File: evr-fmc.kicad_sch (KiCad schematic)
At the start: 0 parts

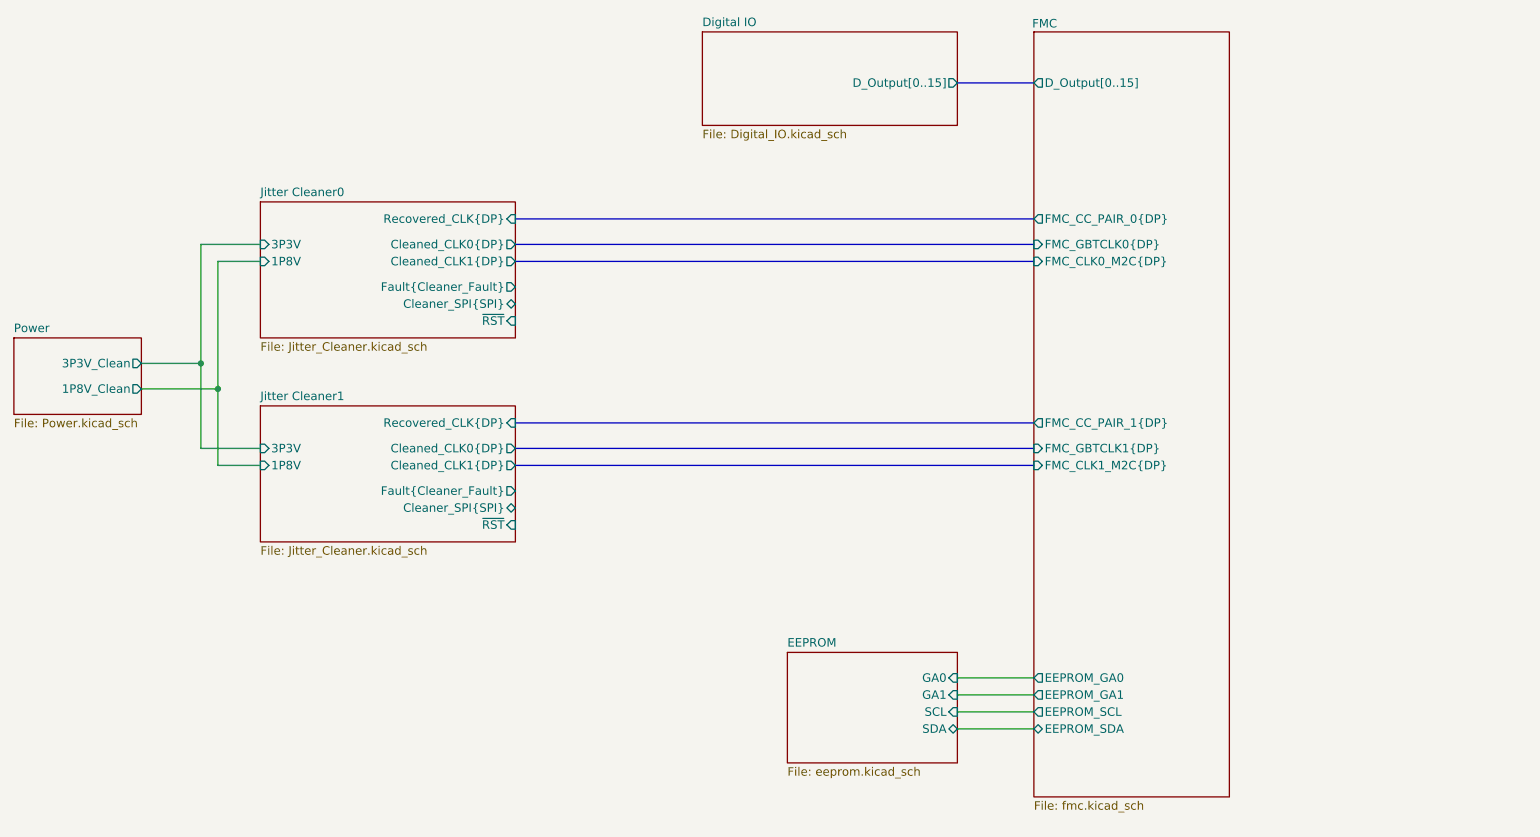
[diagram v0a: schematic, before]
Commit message: Completed Schematic
Completed Schematic Draft
- Includes careful pin mapping to avoid conflicts with other firmwares
- Roughed out LCB layout high speed traces, and FMC breakouts.

Layout and BOM are still WIP
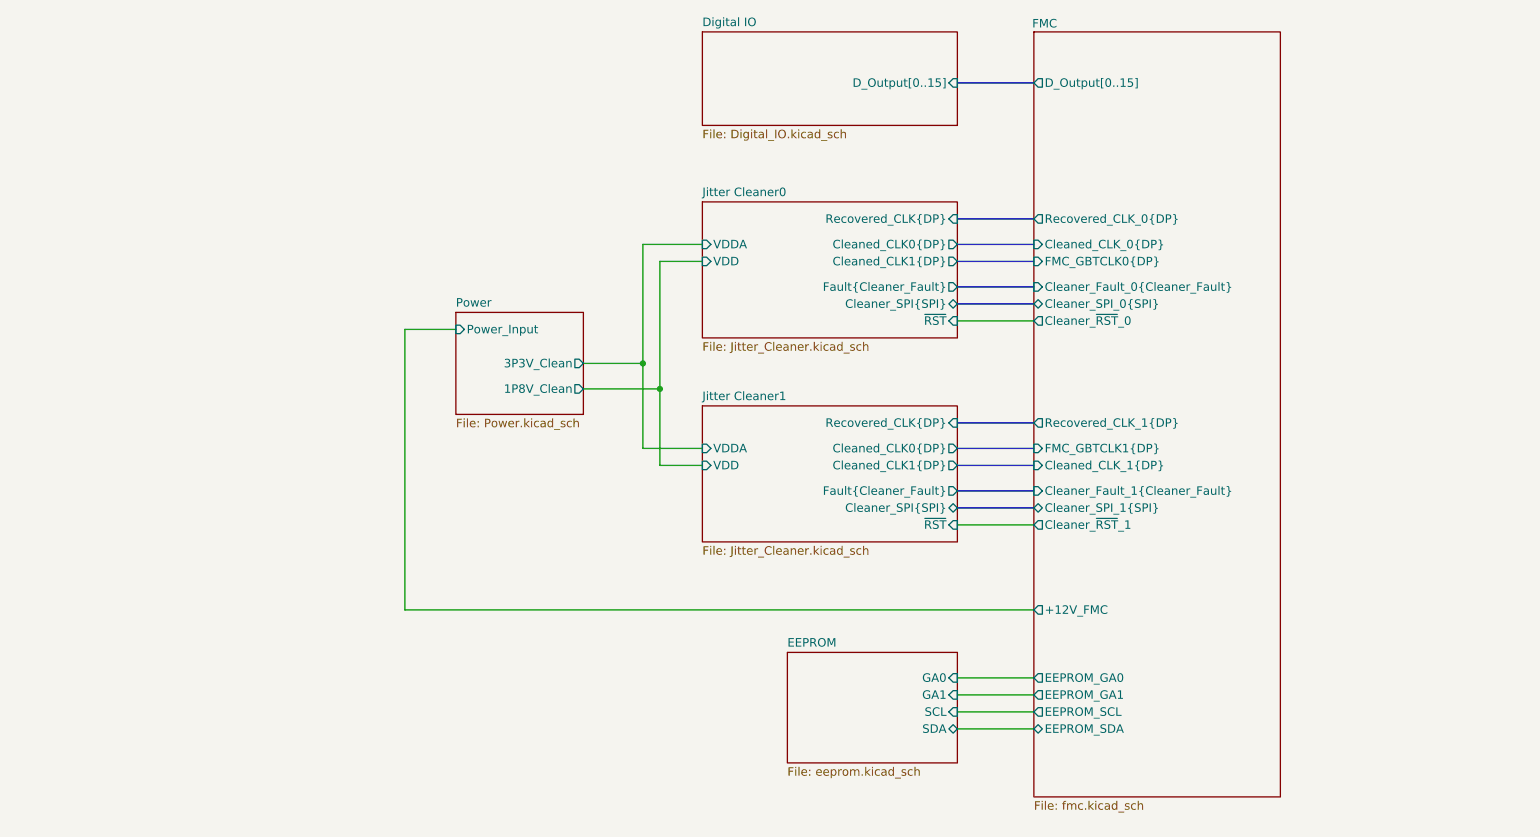
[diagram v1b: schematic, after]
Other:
- sheet FMC ports: added +12V_FMC, Cleaned_CLK_0{DP}, Cleaned_CLK_1{DP}, Cleaner_Fault_0{Cleaner_Fault}, Cleaner_Fault_1{Cleaner_Fault}, Cleaner_SPI_0{SPI}, Cleaner_SPI_1{SPI}, Cleaner_~{RST}_0, Cleaner_~{RST}_1, Recovered_CLK_0{DP}, Recovered_CLK_1{DP}; removed FMC_CC_PAIR_0{DP}, FMC_CC_PAIR_1{DP}, FMC_CLK0_M2C{DP}, FMC_CLK1_M2C{DP}
- sheet Jitter Cleaner0 ports: added VDD, VDDA; removed 1P8V, 3P3V
- sheet Jitter Cleaner1 ports: added VDD, VDDA; removed 1P8V, 3P3V
- sheet Power ports: added Power_Input; removed none

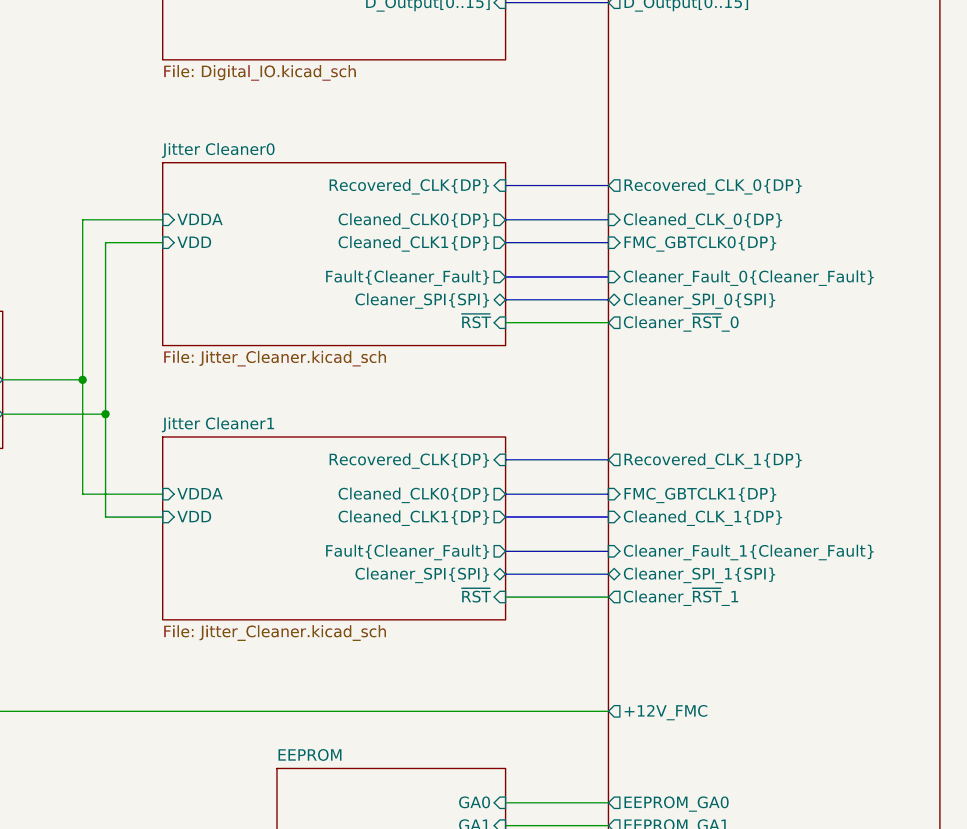
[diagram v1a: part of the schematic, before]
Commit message: Schematic Updates
-Added Heartbeat LED
-Assigned Jitter cleaner OE to FPGA pins
-Changed LDO parts
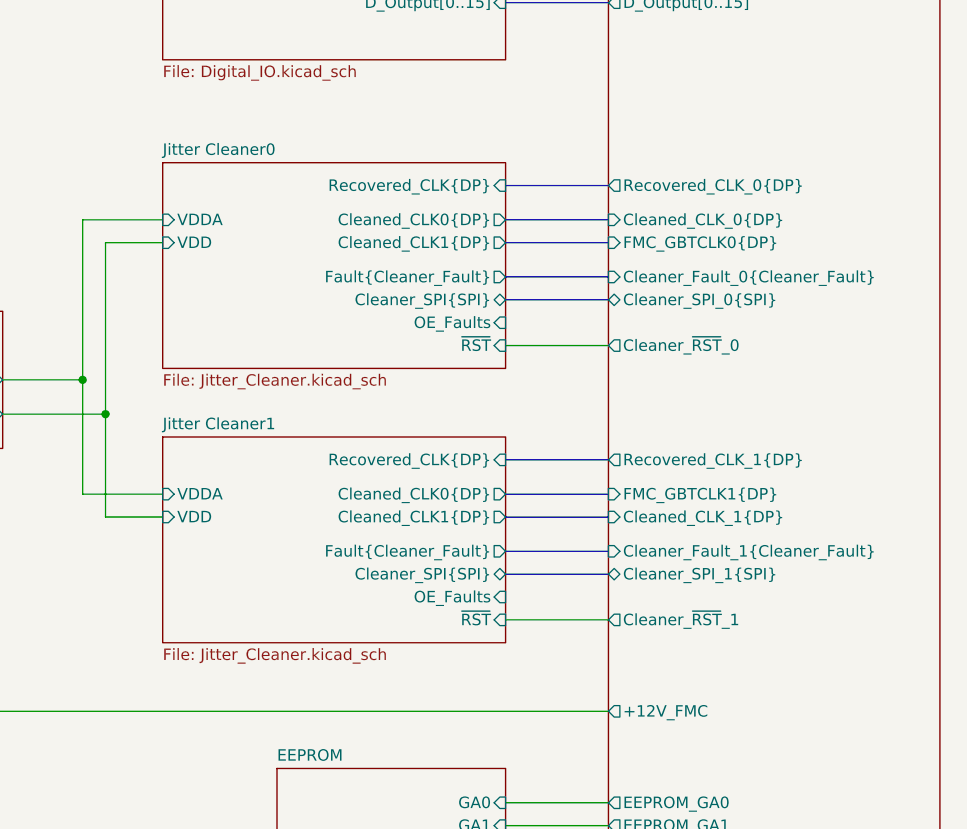
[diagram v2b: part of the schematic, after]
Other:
- sheet Jitter Cleaner0 ports: added OE_Faults; removed none
- sheet Jitter Cleaner1 ports: added OE_Faults; removed none
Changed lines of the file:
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@@
 	(wire
 		(pts
-			(xy 161.29 113.03) (xy 172.72 113.03)
+			(xy 161.29 115.57) (xy 172.72 115.57)
 		)
 		(stroke
@@
 	(wire
 		(pts
-			(xy 161.29 82.55) (xy 172.72 82.55)
+			(xy 161.29 85.09) (xy 172.72 85.09)
 		)
 		(stroke
@@
 	(sheet
 		(at 123.19 95.25)
-		(size 38.1 20.32)
+		(size 38.1 22.86)
 		(exclude_from_sim no)
 		(in_bom yes)
@@
 		)
 		(property "Sheetfile" "Jitter_Cleaner.kicad_sch"
-			(at 123.19 116.1546 0)
+			(at 123.19 118.6946 0)
 			(effects
 				(font
@@
 		)
 		(pin "~{RST}" input
-			(at 161.29 113.03 0)
+			(at 161.29 115.57 0)
 			(effects
 				(font
@@
 				)
 				(justify left)
+			)
+		)
+		(pin "OE_Faults" input
+			(at 161.29 113.03 0)
+			(effects
+				(font
+					(size 1.27 1.27)
+				)
+				(justify right)
 			)
 		)
@@
 	(sheet
 		(at 123.19 64.77)
-		(size 38.1 20.32)
+		(size 38.1 22.86)
 		(exclude_from_sim no)
 		(in_bom yes)
@@
 		)
 		(property "Sheetfile" "Jitter_Cleaner.kicad_sch"
-			(at 123.19 85.6746 0)
+			(at 123.19 88.2146 0)
 			(effects
 				(font
@@
 		)
 		(pin "~{RST}" input
-			(at 161.29 82.55 0)
+			(at 161.29 85.09 0)
 			(effects
 				(font
@@
 				)
 				(justify left)
+			)
+		)
+		(pin "OE_Faults" input
+			(at 161.29 82.55 0)
+			(effects
+				(font
+					(size 1.27 1.27)
+				)
+				(justify right)
 			)
 		)
@@
 		)
 		(pin "Cleaner_~{RST}_0" output
-			(at 172.72 82.55 180)
+			(at 172.72 85.09 180)
 			(effects
 				(font
@@
 		)
 		(pin "Cleaner_~{RST}_1" output
-			(at 172.72 113.03 180)
-			(effects
-				(font
+			(at 172.72 115.57 180)
+			(effects
+				(font

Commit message: Finalized Schematic and Updated Layout
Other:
- sheet Power ports: added 1P8V_Clean_0, 1P8V_Clean_1, 3P3V_Clean_0, 3P3V_Clean_1; removed 1P8V_Clean, 3P3V_Clean
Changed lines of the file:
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@@
 		(members "P" "N")
 	)
-	(junction
-		(at 116.84 92.71)
-		(diameter 0)
-		(color 0 0 0 0)
-	)
-	(junction
-		(at 114.3 88.9)
-		(diameter 0)
-		(color 0 0 0 0)
-	)
 	(wire
 		(pts
@@
 	(wire
 		(pts
-			(xy 123.19 101.6) (xy 114.3 101.6)
-		)
-		(stroke
-			(width 0)
-			(type default)
-		)
-	)
-	(wire
-		(pts
 			(xy 161.29 115.57) (xy 172.72 115.57)
 		)
@@
 	(wire
 		(pts
-			(xy 114.3 88.9) (xy 105.41 88.9)
-		)
-		(stroke
-			(width 0)
-			(type default)
-		)
-	)
-	(wire
-		(pts
-			(xy 114.3 71.12) (xy 114.3 88.9)
-		)
-		(stroke
-			(width 0)
-			(type default)
-		)
-	)
-	(wire
-		(pts
-			(xy 116.84 104.14) (xy 116.84 92.71)
-		)
-		(stroke
-			(width 0)
-			(type default)
-		)
-	)
-	(wire
-		(pts
-			(xy 123.19 104.14) (xy 116.84 104.14)
-		)
-		(stroke
-			(width 0)
-			(type default)
-		)
-	)
-	(wire
-		(pts
-			(xy 114.3 101.6) (xy 114.3 88.9)
+			(xy 114.3 83.82) (xy 105.41 83.82)
+		)
+		(stroke
+			(width 0)
+			(type default)
+		)
+	)
+	(wire
+		(pts
+			(xy 114.3 71.12) (xy 114.3 83.82)
+		)
+		(stroke
+			(width 0)
+			(type default)
+		)
+	)
+	(wire
+		(pts
+			(xy 114.3 95.25) (xy 114.3 104.14)
 		)
 		(stroke
@@
 	(wire
 		(pts
-			(xy 78.74 83.82) (xy 86.36 83.82)
-		)
-		(stroke
-			(width 0)
-			(type default)
-		)
-	)
-	(wire
-		(pts
-			(xy 116.84 73.66) (xy 116.84 92.71)
+			(xy 78.74 80.01) (xy 86.36 80.01)
+		)
+		(stroke
+			(width 0)
+			(type default)
+		)
+	)
+	(wire
+		(pts
+			(xy 116.84 73.66) (xy 116.84 86.36)
+		)
+		(stroke
+			(width 0)
+			(type default)
+		)
+	)
+	(wire
+		(pts
+			(xy 116.84 101.6) (xy 123.19 101.6)
 		)
 		(stroke
@@
 	(wire
 		(pts
+			(xy 114.3 104.14) (xy 123.19 104.14)
+		)
+		(stroke
+			(width 0)
+			(type default)
+		)
+	)
+	(wire
+		(pts
 			(xy 161.29 140.97) (xy 172.72 140.97)
 		)
@@
 	(wire
 		(pts
-			(xy 116.84 92.71) (xy 105.41 92.71)
+			(xy 116.84 86.36) (xy 105.41 86.36)
 		)
 		(stroke
@@
 	(wire
 		(pts
-			(xy 78.74 125.73) (xy 78.74 83.82)
+			(xy 78.74 125.73) (xy 78.74 80.01)
+		)
+		(stroke
+			(width 0)
+			(type default)
+		)
+	)
+	(wire
+		(pts
+			(xy 105.41 92.71) (xy 116.84 92.71)
 		)
 		(stroke
@@
 		)
 	)
+	(wire
+		(pts
+			(xy 116.84 92.71) (xy 116.84 101.6)
+		)
+		(stroke
+			(width 0)
+			(type default)
+		)
+	)
 	(bus
 		(pts
@@
 		(pts
 			(xy 161.29 71.12) (xy 172.72 71.12)
+		)
+		(stroke
+			(width 0)
+			(type default)
+		)
+	)
+	(wire
+		(pts
+			(xy 105.41 95.25) (xy 114.3 95.25)
 		)
 		(stroke
@@
 	)
 	(sheet
-		(at 86.36 81.28)
-		(size 19.05 15.24)
+		(at 86.36 77.47)
+		(size 19.05 21.59)
 		(exclude_from_sim no)
 		(in_bom yes)
@@
 		)
 		(property "Sheetname" "Power"
-			(at 86.36 80.5684 0)
+			(at 86.36 76.7584 0)
 			(effects
 				(font
@@
 		)
 		(property "Sheetfile" "Power.kicad_sch"
-			(at 86.36 97.1046 0)
+			(at 86.36 99.6446 0)
 			(effects
 				(font
@@
 			)
 		)
-		(pin "1P8V_Clean" output
+		(pin "Power_Input" input
+			(at 86.36 80.01 180)
+			(effects
+				(font
+					(size 1.27 1.27)
+				)
+				(justify left)
+			)
+		)
+		(pin "1P8V_Clean_0" output
+			(at 105.41 86.36 0)
+			(effects
+				(font
+					(size 1.27 1.27)
+				)
+				(justify right)
+			)
+		)
+		(pin "1P8V_Clean_1" output
+			(at 105.41 95.25 0)
+			(effects
+				(font
+					(size 1.27 1.27)
+				)
+				(justify right)
+			)
+		)
+		(pin "3P3V_Clean_0" output
+			(at 105.41 83.82 0)
+			(effects
+				(font
+					(size 1.27 1.27)
+				)
+				(justify right)
+			)
+		)
+		(pin "3P3V_Clean_1" output
 			(at 105.41 92.71 0)
 			(effects
@@
 			)
 		)
-		(pin "3P3V_Clean" output
-			(at 105.41 88.9 0)
-			(effects
-				(font
-					(size 1.27 1.27)
-				)
-				(justify right)
-			)
-		)
-		(pin "Power_Input" input
-			(at 86.36 83.82 180)
-			(effects
-				(font
-					(size 1.27 1.27)
-				)
-				(justify left)
-			)
-		)

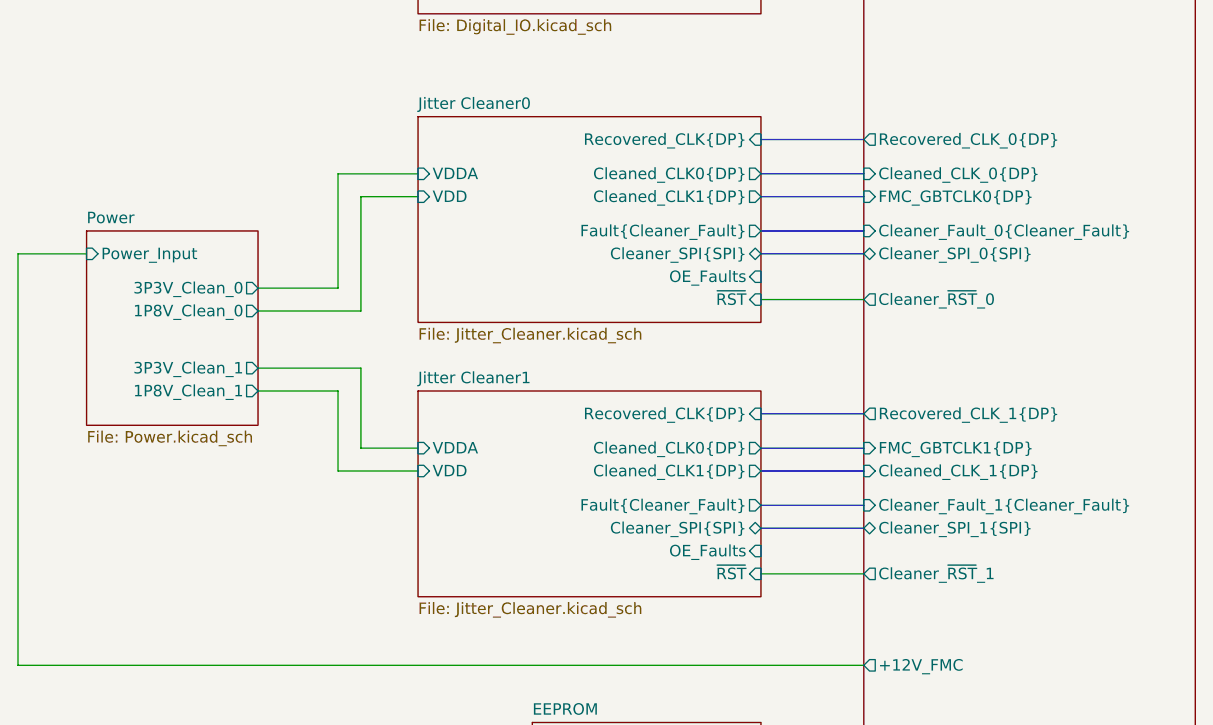
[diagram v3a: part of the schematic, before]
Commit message: Draft Layout Complete
-Draft Layout Complete
- Silkscreen need to be complete
- some Digital IO swapped FMC pins
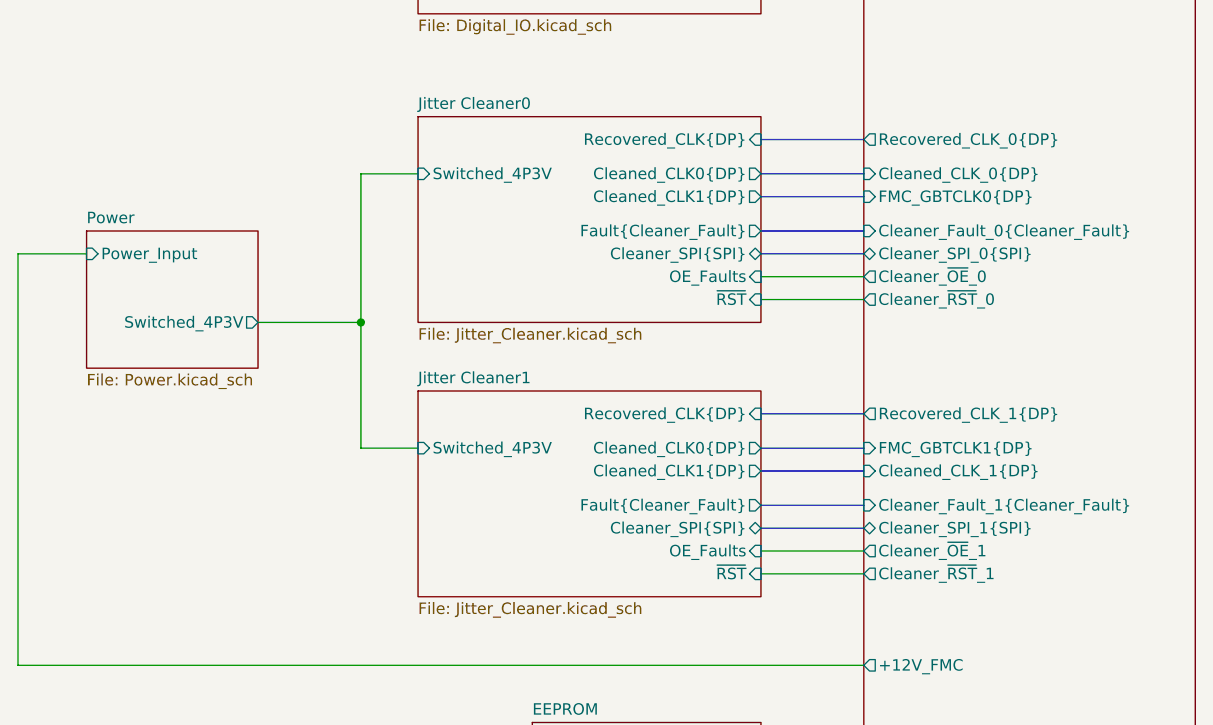
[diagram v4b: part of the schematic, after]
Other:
- sheet FMC ports: added Cleaner_~{OE}_0, Cleaner_~{OE}_1; removed none
- sheet Jitter Cleaner0 ports: added Switched_4P3V; removed VDD, VDDA
- sheet Jitter Cleaner1 ports: added Switched_4P3V; removed VDD, VDDA
- sheet Power ports: added Switched_4P3V; removed 1P8V_Clean_0, 1P8V_Clean_1, 3P3V_Clean_0, 3P3V_Clean_1
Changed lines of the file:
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@@
 		(members "P" "N")
 	)
+	(junction
+		(at 116.84 87.63)
+		(diameter 0)
+		(color 0 0 0 0)
+	)
 	(wire
 		(pts
@@
 	(wire
 		(pts
-			(xy 114.3 83.82) (xy 105.41 83.82)
-		)
-		(stroke
-			(width 0)
-			(type default)
-		)
-	)
-	(wire
-		(pts
-			(xy 114.3 71.12) (xy 114.3 83.82)
-		)
-		(stroke
-			(width 0)
-			(type default)
-		)
-	)
-	(wire
-		(pts
-			(xy 114.3 95.25) (xy 114.3 104.14)
+			(xy 116.84 71.12) (xy 116.84 87.63)
 		)
 		(stroke
@@
 	(wire
 		(pts
-			(xy 123.19 71.12) (xy 114.3 71.12)
+			(xy 123.19 71.12) (xy 116.84 71.12)
 		)
 		(stroke
@@
 	(wire
 		(pts
-			(xy 116.84 73.66) (xy 116.84 86.36)
+			(xy 161.29 82.55) (xy 172.72 82.55)
 		)
 		(stroke
@@
 		)
 	)
-	(wire
-		(pts
-			(xy 123.19 73.66) (xy 116.84 73.66)
-		)
-		(stroke
-			(width 0)
-			(type default)
-		)
-	)
 	(bus
 		(pts
@@
 	(wire
 		(pts
-			(xy 114.3 104.14) (xy 123.19 104.14)
-		)
-		(stroke
-			(width 0)
-			(type default)
-		)
-	)
-	(wire
-		(pts
 			(xy 161.29 140.97) (xy 172.72 140.97)
 		)
@@
 	(wire
 		(pts
-			(xy 116.84 86.36) (xy 105.41 86.36)
-		)
-		(stroke
-			(width 0)
-			(type default)
-		)
-	)
-	(wire
-		(pts
 			(xy 172.72 125.73) (xy 78.74 125.73)
 		)
@@
 	(wire
 		(pts
-			(xy 105.41 92.71) (xy 116.84 92.71)
+			(xy 105.41 87.63) (xy 116.84 87.63)
 		)
 		(stroke
@@
 	(wire
 		(pts
-			(xy 116.84 92.71) (xy 116.84 101.6)
+			(xy 116.84 87.63) (xy 116.84 101.6)
+		)
+		(stroke
+			(width 0)
+			(type default)
+		)
+	)
+	(wire
+		(pts
+			(xy 161.29 113.03) (xy 172.72 113.03)
 		)
 		(stroke
@@
 		(pts
 			(xy 161.29 71.12) (xy 172.72 71.12)
-		)
-		(stroke
-			(width 0)
-			(type default)
-		)
-	)
-	(wire
-		(pts
-			(xy 105.41 95.25) (xy 114.3 95.25)
 		)
 		(stroke
@@
 			)
 		)
-		(pin "VDD" input
-			(at 123.19 104.14 180)
-			(effects
-				(font
-					(size 1.27 1.27)
-				)
-				(justify left)
-			)
-		)
-		(pin "VDDA" input
-			(at 123.19 101.6 180)
-			(effects
-				(font
-					(size 1.27 1.27)
-				)
-				(justify left)
-			)
-		)
 		(pin "OE_Faults" input
 			(at 161.29 113.03 0)
@@
 				)
 				(justify right)
+			)
+		)
+		(pin "Switched_4P3V" input
+			(at 123.19 101.6 180)
+			(effects
+				(font
+					(size 1.27 1.27)
+				)
+				(justify left)
 			)
 		)
@@
 			)
 		)
-		(pin "VDD" input
-			(at 123.19 73.66 180)
-			(effects
-				(font
-					(size 1.27 1.27)
-				)
-				(justify left)
-			)
-		)
-		(pin "VDDA" input
-			(at 123.19 71.12 180)
-			(effects
-				(font
-					(size 1.27 1.27)
-				)
-				(justify left)
-			)
-		)
 		(pin "OE_Faults" input
 			(at 161.29 82.55 0)
@@
 				)
 				(justify right)
+			)
+		)
+		(pin "Switched_4P3V" input
+			(at 123.19 71.12 180)
+			(effects
+				(font
+					(size 1.27 1.27)
+				)
+				(justify left)
 			)
 		)
@@
 			)
 		)
+		(pin "Cleaner_~{OE}_0" output
+			(at 172.72 82.55 180)
+			(effects
+				(font
+					(size 1.27 1.27)
+				)
+				(justify left)
+			)
+		)
+		(pin "Cleaner_~{OE}_1" output
+			(at 172.72 113.03 180)
+			(effects
+				(font
+					(size 1.27 1.27)
+				)
+				(justify left)
+			)
+		)
 		(instances
 			(project "evr-fmc"
@@
 	(sheet
 		(at 86.36 77.47)
-		(size 19.05 21.59)
+		(size 19.05 15.24)
 		(exclude_from_sim no)
 		(in_bom yes)
@@
 		)
 		(property "Sheetfile" "Power.kicad_sch"
-			(at 86.36 99.6446 0)
+			(at 86.36 93.2946 0)
 			(effects
 				(font
@@
 			)
 		)
-		(pin "1P8V_Clean_0" output
-			(at 105.41 86.36 0)
-			(effects
-				(font
-					(size 1.27 1.27)
-				)
-				(justify right)
-			)
-		)
-		(pin "1P8V_Clean_1" output
-			(at 105.41 95.25 0)
-			(effects
-				(font
-					(size 1.27 1.27)
-				)
-				(justify right)
-			)
-		)
-		(pin "3P3V_Clean_0" output
-			(at 105.41 83.82 0)
-			(effects
-				(font
-					(size 1.27 1.27)
-				)
-				(justify right)
-			)
-		)
-		(pin "3P3V_Clean_1" output
-			(at 105.41 92.71 0)
-			(effects
-				(font
+		(pin "Switched_4P3V" output
+			(at 105.41 87.63 0)
+			(effects
+				(font
